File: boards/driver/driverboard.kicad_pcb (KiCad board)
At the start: 2 copper layers, 49.5 x 54.6 mm, 44 parts, among them J1 RJ45, J2 RJ45, P1 HE10-10, Q1 NDS355, Q2 NDS355, Q3 NDS355, Q4 NDS355, Q5 NDS355, Q6 NDS355, Q7 NDS355, Q8 NDS355, U1 74HC595, U2 TS2937

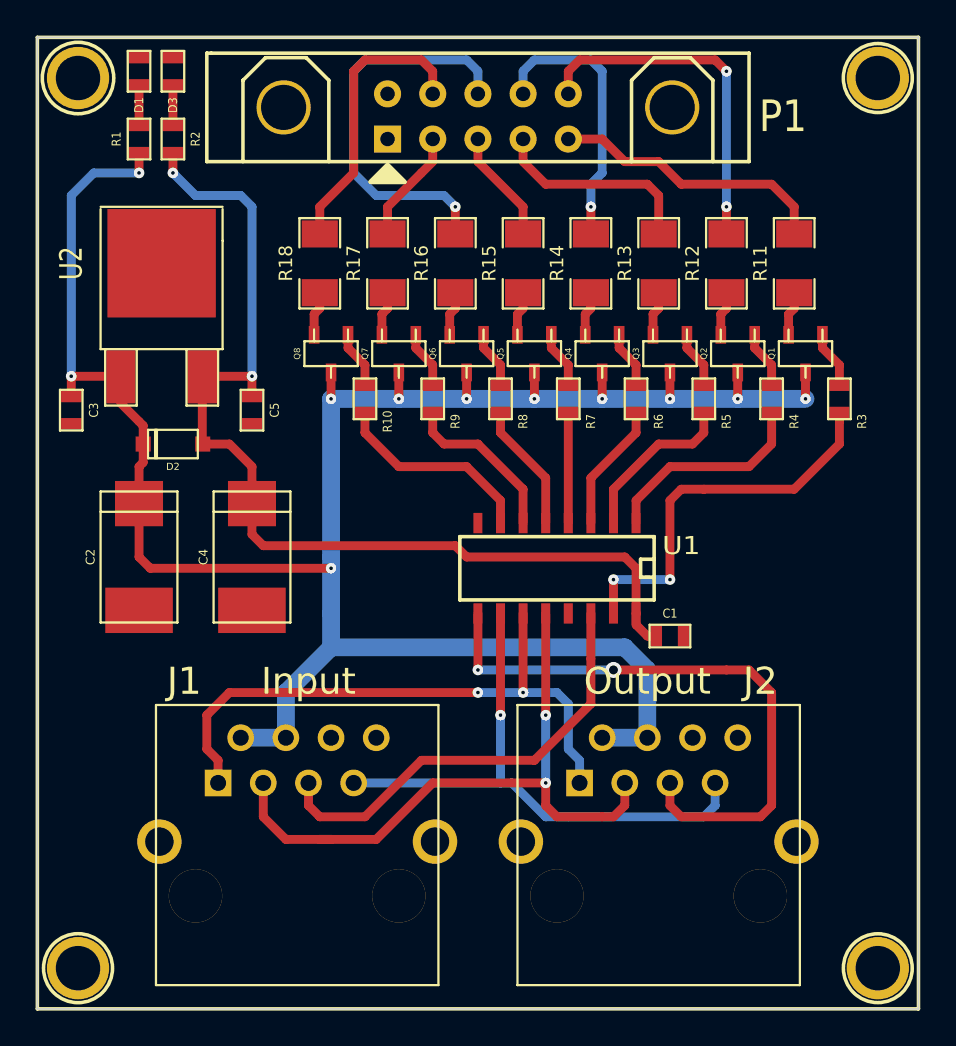
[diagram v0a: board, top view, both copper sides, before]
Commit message: Updated driverboard layout
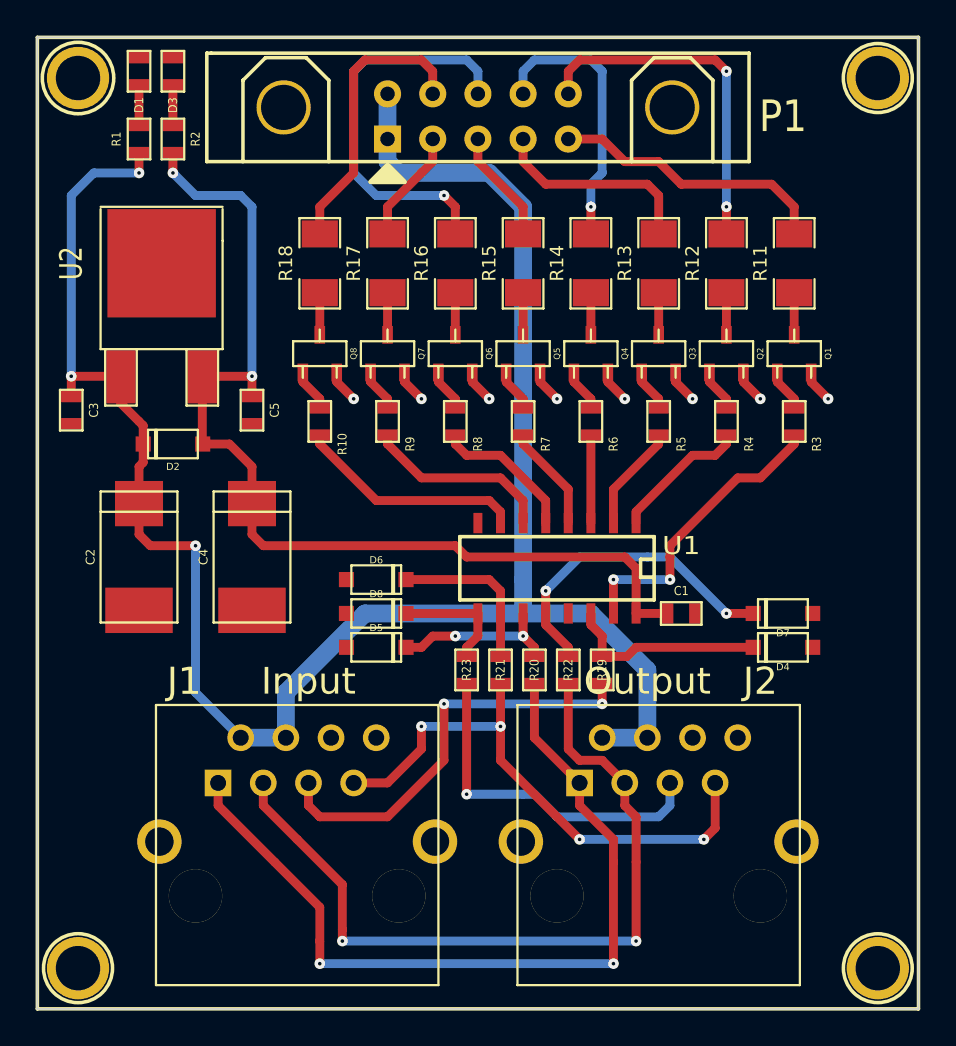
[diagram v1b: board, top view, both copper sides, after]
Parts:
- added D4: ZENER, sod123, F.Cu at (141.6, 68.6)
- added D5: ZENER, sod123, F.Cu at (118.7, 68.6)
- added D6: ZENER, sod123, F.Cu at (118.7, 64.8)
- added D7: ZENER, sod123, F.Cu at (141.6, 66.7)
- added D8: ZENER, sod123, F.Cu at (118.7, 66.7)
- added R19: 1k, SM0603, F.Cu at (131.4, 69.8)
- added R20: 1k, SM0603, F.Cu at (127.6, 69.8)
- added R21: 1k, SM0603, F.Cu at (125.7, 69.8)
- added R22: 1k, SM0603, F.Cu at (129.5, 69.8)
- added R23: 1k, SM0603, F.Cu at (123.8, 69.8)
- R10, R3, R4, R5, R6, R7, R8, R9: value 200 -> 220
- moved G*** 4.75 mm to (128.3, 52.7)
- moved R10 2.84 mm to (115.6, 55.9)
- moved R8 2.84 mm to (123.2, 55.9)
- moved R9 2.84 mm to (119.4, 55.9)
- moved R3 2.84 mm to (142.2, 55.9)
- moved R4 2.84 mm to (138.4, 55.9)
- moved R5 2.84 mm to (134.6, 55.9)
- moved R6 2.84 mm to (130.8, 55.9)
- moved R7 2.84 mm to (127.0, 55.9)
- moved C1 1.42 mm to (135.9, 66.7)
- moved Q5 0.64 mm to (127.0, 52.1), turned to 0 degrees
- moved Q6 0.64 mm to (123.2, 52.1), turned to 0 degrees
- moved Q7 0.64 mm to (119.4, 52.1), turned to 0 degrees
- moved Q8 0.64 mm to (115.6, 52.1), turned to 0 degrees
- moved Q1 0.63 mm to (142.2, 52.1), turned to 0 degrees
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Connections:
- P1 pad 1: GND -> +24V
- P1 pad 2: GND -> +24V
- Q1 pad 2: +24V -> N-0000022
- Q1 pad 3: N-0000011 -> GND
- Q2 pad 2: +24V -> N-0000024
- Q2 pad 3: N-0000022 -> GND
- Q3 pad 2: +24V -> N-0000019
- Q3 pad 3: N-000003 -> GND
- Q4 pad 2: +24V -> N-0000017
- Q4 pad 3: N-000005 -> GND
- Q5 pad 2: +24V -> N-0000025
- Q5 pad 3: N-000007 -> GND
- Q6 pad 2: +24V -> N-0000027
- Q6 pad 3: N-0000010 -> GND
- Q7 pad 2: +24V -> N-0000036
- Q7 pad 3: N-0000034 -> GND
- Q8 pad 2: +24V -> N-0000034
- Q8 pad 3: N-0000037 (its old number) -> GND
- R11 pad 1: N-0000011 -> N-0000022
- R12 pad 1: N-0000022 -> N-0000024
- R13 pad 1: N-000003 -> N-0000019
- R14 pad 1: N-000005 -> N-0000017
- R15 pad 1: N-000007 -> N-0000025
- R16 pad 1: N-0000010 -> N-0000027
- R17 pad 1: N-0000034 -> N-0000036
- R18 pad 1: N-0000037 (its old number) -> N-0000034
- U1 pad 10: Reset -> N-0000029
- U1 pad 11: Clock -> N-0000030
- U1 pad 12: Enable -> N-0000033
- U1 pad 14: Data_In -> N-0000032
- U1 pad 9: Data_Out -> N-0000031
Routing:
- net N-0000033: track 0.00 -> 18.0 mm, vias 0 -> 2
- net GND: track 0.00 -> 15.0 mm, vias 0 -> 8
- net Data_Out: track 34.1 -> 19.7 mm, vias 2 -> 1
- net +24V: track 127.2 -> 114.6 mm, vias 11 -> 3
- net Clock: track 34.3 -> 46.6 mm
- net N-0000032: track 0.00 -> 11.4 mm
- net N-0000030: track 0.00 -> 9.52 mm, vias 0 -> 2
- net N-0000029: track 0.00 -> 9.26 mm
- net Enable: track 37.3 -> 44.0 mm
- net N-0000031: track 0.00 -> 6.72 mm
- net FET_1: track 22.1 -> 16.8 mm
- net FET_2: track 12.0 -> 7.80 mm
- net FET_3: track 9.44 -> 6.01 mm
- net N-000007: track 2.50 -> 0.00 mm
- net N-000005: track 2.50 -> 0.00 mm
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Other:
- board text added: "Version 1.1"
- board text removed: "Version 1.0"

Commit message: Minor Silkscreen fixes
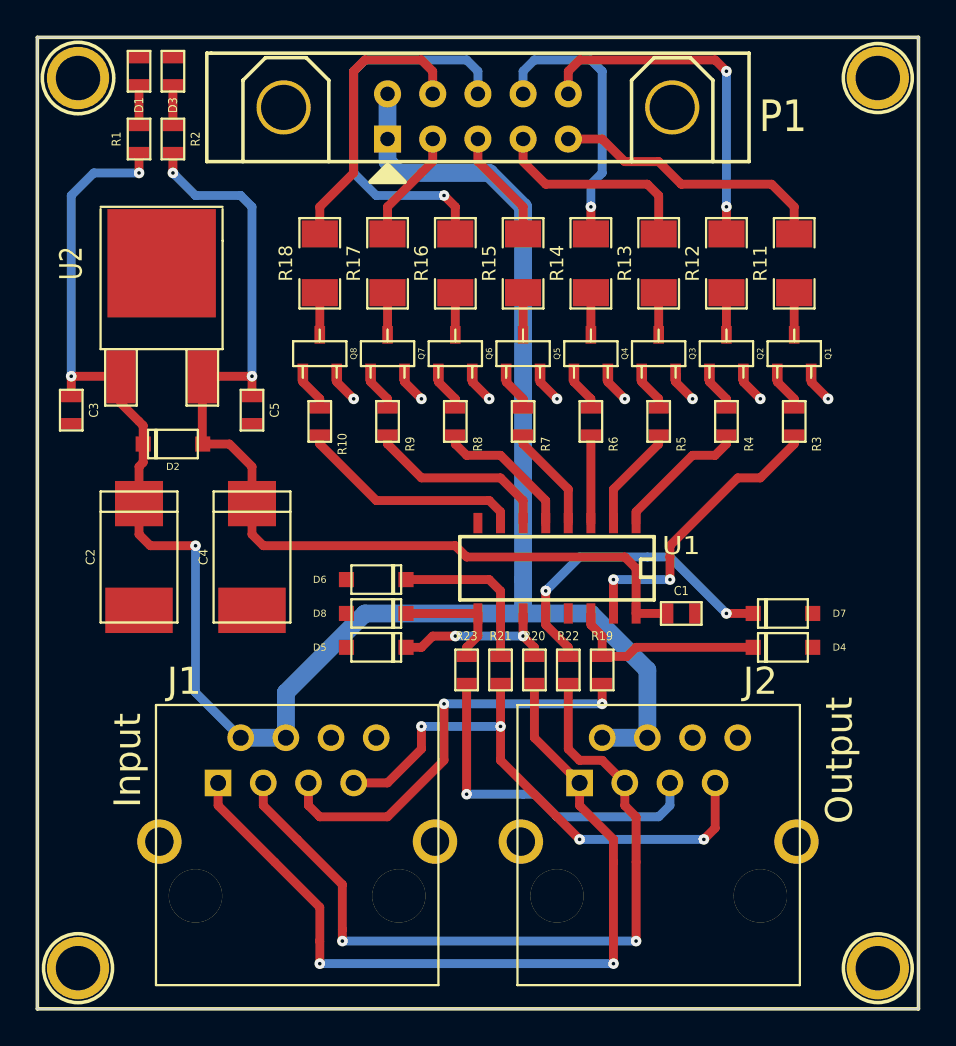
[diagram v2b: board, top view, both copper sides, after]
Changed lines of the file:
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@@
   (page A3)
   (layers
-    (15 F.Cu signal hide)
-    (0 B.Cu signal)
+    (15 F.Cu signal)
+    (0 B.Cu signal hide)
     (16 B.Adhes user)
     (17 F.Adhes user hide)
     (18 B.Paste user)
     (19 F.Paste user)
-    (20 B.SilkS user)
+    (20 B.SilkS user hide)
     (21 F.SilkS user)
     (22 B.Mask user)
@@
   )
   (setup
-    (last_trace_width 0.5)
+    (last_trace_width 0.254)
     (user_trace_width 0.3)
     (user_trace_width 0.5)
@@
     (at 141.605 68.58 180)
     (descr SOD123)
-    (fp_text reference D4 (at 0 -1.09982 180) (layer F.SilkS)
+    (fp_text reference D4 (at -3.175 0 180) (layer F.SilkS)
       (effects (font (size 0.39878 0.39878) (thickness 0.09906)))
     )
@@
     (at 118.745 68.58)
     (descr SOD123)
-    (fp_text reference D5 (at 0 -1.09982) (layer F.SilkS)
+    (fp_text reference D5 (at -3.175 0) (layer F.SilkS)
       (effects (font (size 0.39878 0.39878) (thickness 0.09906)))
     )
@@
     (at 118.745 64.77)
     (descr SOD123)
-    (fp_text reference D6 (at 0 -1.09982) (layer F.SilkS)
+    (fp_text reference D6 (at -3.175 0) (layer F.SilkS)
       (effects (font (size 0.39878 0.39878) (thickness 0.09906)))
     )
@@
     (at 141.605 66.675 180)
     (descr SOD123)
-    (fp_text reference D7 (at 0 -1.09982 180) (layer F.SilkS)
+    (fp_text reference D7 (at -3.175 0 180) (layer F.SilkS)
       (effects (font (size 0.39878 0.39878) (thickness 0.09906)))
     )
@@
     (at 118.745 66.675)
     (descr SOD123)
-    (fp_text reference D8 (at 0 -1.09982) (layer F.SilkS)
+    (fp_text reference D8 (at -3.175 0) (layer F.SilkS)
       (effects (font (size 0.39878 0.39878) (thickness 0.09906)))
     )
@@
     (at 131.445 69.85 90)
     (attr smd)
-    (fp_text reference R19 (at 0 0 90) (layer F.SilkS)
+    (fp_text reference R19 (at 1.905 0 180) (layer F.SilkS)
       (effects (font (size 0.508 0.4572) (thickness 0.1143)))
     )
@@
     (at 127.635 69.85 90)
     (attr smd)
-    (fp_text reference R20 (at 0 0 90) (layer F.SilkS)
+    (fp_text reference R20 (at 1.905 0 180) (layer F.SilkS)
       (effects (font (size 0.508 0.4572) (thickness 0.1143)))
     )
@@
     (at 125.73 69.85 90)
     (attr smd)
-    (fp_text reference R21 (at 0 0 90) (layer F.SilkS)
+    (fp_text reference R21 (at 1.905 0 180) (layer F.SilkS)
       (effects (font (size 0.508 0.4572) (thickness 0.1143)))
     )
@@
     (at 129.54 69.85 90)
     (attr smd)
-    (fp_text reference R22 (at 0 0 90) (layer F.SilkS)
+    (fp_text reference R22 (at 1.905 0 180) (layer F.SilkS)
       (effects (font (size 0.508 0.4572) (thickness 0.1143)))
     )
@@
     (at 123.825 69.85 270)
     (attr smd)
-    (fp_text reference R23 (at 0 0 270) (layer F.SilkS)
+    (fp_text reference R23 (at -1.905 0 360) (layer F.SilkS)
       (effects (font (size 0.508 0.4572) (thickness 0.1143)))
     )
@@
     (effects (font (size 1 1) (thickness 0.25)) (justify mirror))
   )
-  (gr_text Output (at 133.985 70.485) (layer F.SilkS)
+  (gr_text Output (at 144.78 74.93 90) (layer F.SilkS)
     (effects (font (size 1.5 1.5) (thickness 0.3)))
   )
-  (gr_text Input (at 114.935 70.485) (layer F.SilkS)
+  (gr_text Input (at 104.775 74.93 90) (layer F.SilkS)
     (effects (font (size 1.5 1.5) (thickness 0.3)))
   )

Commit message: Final fixes to board layouts
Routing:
- net N-0000033: track 18.0 -> 16.4 mm
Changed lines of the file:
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@@
     (thickness 1.6)
     (drawings 35)
-    (tracks 316)
+    (tracks 315)
     (zones 0)
     (modules 54)
@@
   (layers
     (15 F.Cu signal)
-    (0 B.Cu signal hide)
+    (0 B.Cu signal)
     (16 B.Adhes user)
     (17 F.Adhes user hide)
@@
     (21 F.SilkS user)
     (22 B.Mask user)
-    (23 F.Mask user)
+    (23 F.Mask user hide)
     (24 Dwgs.User user)
     (25 Cmts.User user hide)
@@
   )
   (setup
-    (last_trace_width 0.254)
+    (last_trace_width 0.5)
     (user_trace_width 0.3)
     (user_trace_width 0.5)
@@
     (pcbplotparams
       (layerselection 272400385)
-      (usegerberextensions true)
+      (usegerberextensions false)
       (excludeedgelayer true)
       (linewidth 0.150000)
@@
       (plotinvisibletext false)
       (padsonsilk false)
-      (subtractmaskfromsilk true)
-      (outputformat 1)
+      (subtractmaskfromsilk false)
+      (outputformat 2)
       (mirror false)
-      (drillshape 0)
+      (drillshape 2)
       (scaleselection 1)
-      (outputdirectory gerber/))
+      (outputdirectory plot/))
   )
   (net 0 "")
@@
   (segment (start 131.445 67.945) (end 131.445 69.088) (width 0.5) (layer F.Cu) (net 30))
   (segment (start 130.81 67.31) (end 131.445 67.945) (width 0.5) (layer F.Cu) (net 30))
+  (segment (start 128.27 65.405) (end 131.445 65.405) (width 0.5) (layer B.Cu) (net 31))
+  (segment (start 132.715 66.675) (end 138.43 66.675) (width 0.5) (layer B.Cu) (net 31))
+  (segment (start 131.445 65.405) (end 132.715 66.675) (width 0.5) (layer B.Cu) (net 31))
   (via (at 138.43 66.675) (size 0.6) (drill 0.2) (layers F.Cu B.Cu) (net 31))
-  (segment (start 135.255 63.5) (end 138.43 66.675) (width 0.5) (layer B.Cu) (net 31))
   (segment (start 128.27 66.675) (end 128.27 65.405) (width 0.5) (layer F.Cu) (net 31))
-  (segment (start 130.175 63.5) (end 133.985 63.5) (width 0.5) (layer B.Cu) (net 31))
-  (segment (start 128.27 65.405) (end 130.175 63.5) (width 0.5) (layer B.Cu) (net 31))
   (via (at 128.27 65.405) (size 0.6) (drill 0.2) (layers F.Cu B.Cu) (net 31))
-  (segment (start 133.985 63.5) (end 135.255 63.5) (width 0.5) (layer B.Cu) (net 31))
   (segment (start 138.43 66.675) (end 139.93114 66.675) (width 0.5) (layer F.Cu) (net 31))
   (segment (start 128.27 66.675) (end 128.27 67.31) (width 0.5) (layer F.Cu) (net 31))

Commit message: Added logos
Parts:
- added G***: logo_hacker_silkbot_10_00mm, logo_hacker_silkbot_10_00mm, B.Cu at (113.7, 66.7)
